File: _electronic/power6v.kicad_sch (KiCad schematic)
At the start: 19 parts

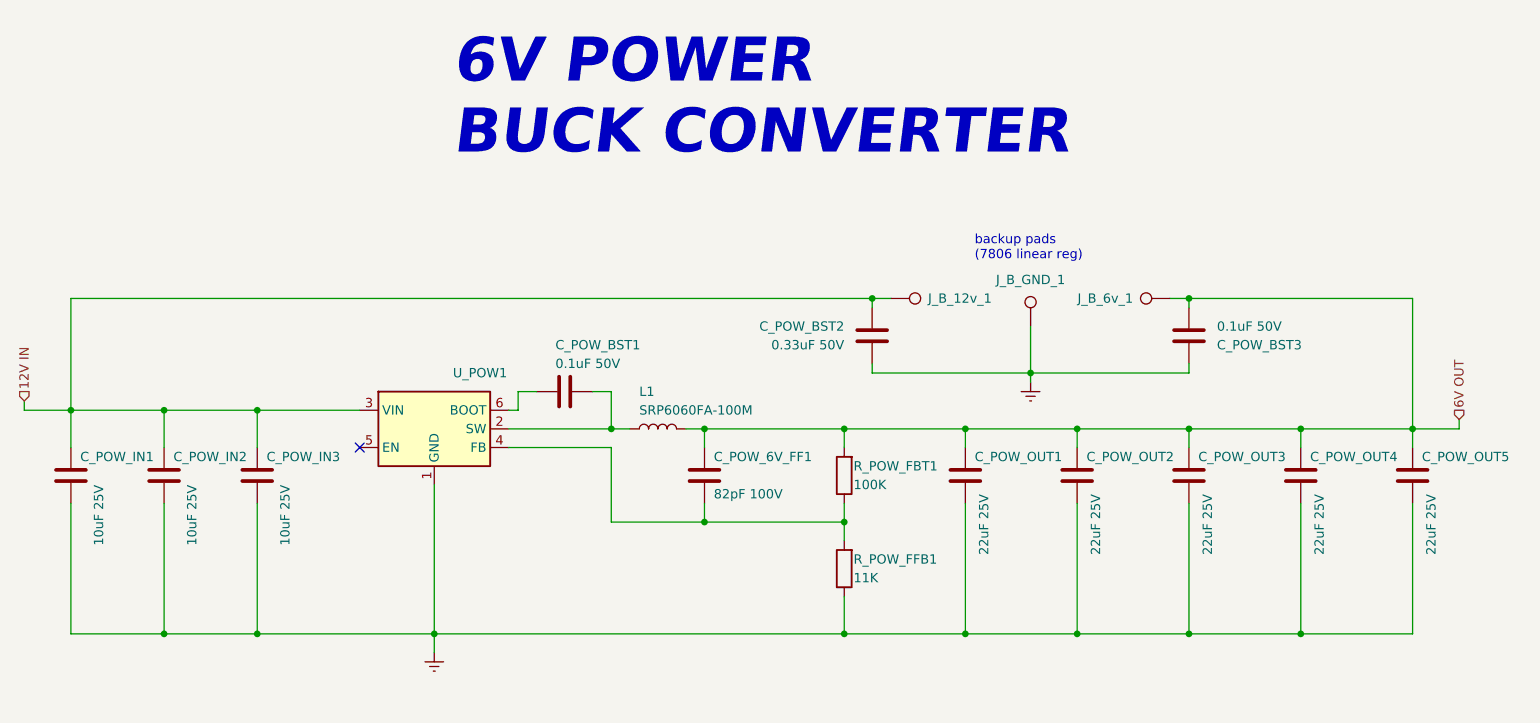
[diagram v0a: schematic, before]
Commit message: led resistor revision, b.o.m. and pcb anotation
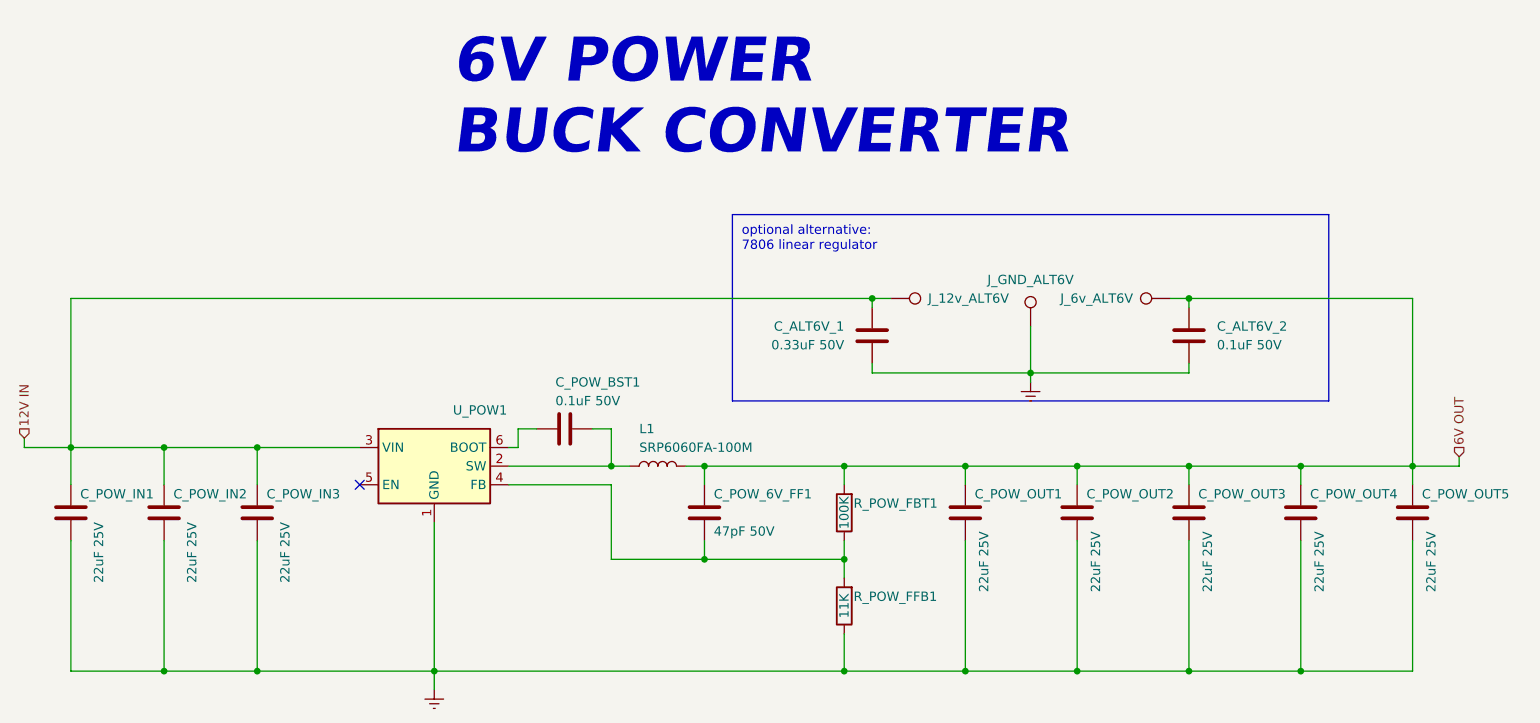
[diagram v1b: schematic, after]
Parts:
- C_ALT6V_1: renamed from C_POW_BST2; now left out of the parts list
- C_ALT6V_2: renamed from C_POW_BST3; now left out of the parts list
- C_POW_6V_FF1: value 82pF 100V -> 47pF 50V; # VJ0603A820JXBAC -> CGA3E2C0G1H470J080AA
- C_POW_IN1, C_POW_IN2, C_POW_IN3: value 10uF 25V -> 22uF 25V; # (none) -> C3225X7R1E226M250AB
- R_POW_FBT1: # CHP0603AFX-1003ELF -> ERJ-3EKF1003V
- R_POW_FFB1: # CRCW060311K0JNEAHP -> ERJ-3EKF1102V
- renumbered J_B_12v_1 to J_12v_ALT6V, J_B_6v_1 to J_6v_ALT6V, J_B_GND_1 to J_GND_ALT6V
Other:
- note added: "optional alternative: 7806 linear regulator"
- note removed: "backup pads (7806 linear reg)"
- moved on the sheet: C_POW_6V_FF1, C_POW_BST1, C_POW_IN1, C_POW_IN2, C_POW_IN3, C_POW_OUT1, C_POW_OUT2, C_POW_OUT3, C_POW_OUT4, C_POW_OUT5, L1, R_POW_FBT1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

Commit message: schematics and pcb cleanup
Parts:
- renumbered J_12v_ALT6V to J_12v_ALT6V1, J_6v_ALT6V to J_6v_ALT6V1, J_GND_ALT6V to J_GND_ALT6V1
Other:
- note added: "alternative 6V output: 7806 linear regulator"
- note removed: "optional alternative: 7806 linear regulator"
- title: E-TKT -> E-TKT v1.0
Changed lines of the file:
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@@
   (paper "A4")
   (title_block
-    (title "E-TKT")
-    (date "2022-07-21")
-    (rev "3")
+    (title "E-TKT v1.0")
+    (date "2022-09-29")
+    (rev "4")
     (company "Andrei Speridiao")
   )
@@
     (stroke (width 0) (type default) (color 0 0 0 0))
   )
-  (text "optional alternative:\n7806 linear regulator" (at 149.86 67.31 0)
+  (text "alternative 6V output:\n7806 linear regulator" (at 149.86 67.31 0)
     (effects (font (size 1.27 1.27)) (justify left bottom))
   )
@@
   (symbol (lib_id "Connector:TestPoint") (at 170.18 73.66 270) (unit 1)
     (in_bom yes) (on_board yes)
-    (property "Reference" "J_12v_ALT6V" (id 0) (at 175.26 73.66 90)
+    (property "Reference" "J_12v_ALT6V1" (id 0) (at 175.26 73.66 90)
       (effects (font (size 1.27 1.27)) (justify left))
     )
@@
   (symbol (lib_id "Connector:TestPoint") (at 189.23 77.47 0) (unit 1)
     (in_bom yes) (on_board yes)
-    (property "Reference" "J_GND_ALT6V" (id 0) (at 189.23 71.12 0))
+    (property "Reference" "J_GND_ALT6V1" (id 0) (at 189.23 71.12 0))
     (property "Value" "TestPoint" (id 1) (at 189.23 72.39 90)
       (effects (font (size 1.27 1.27)) (justify left) hide)
@@
   (symbol (lib_id "Connector:TestPoint") (at 208.28 73.66 90) (unit 1)
     (in_bom yes) (on_board yes)
-    (property "Reference" "J_6v_ALT6V" (id 0) (at 203.2 73.66 90)
-      (effects (font (size 1.27 1.27)) (justify left))
-    )
+    (property "Reference" "J_6v_ALT6V1" (id 0) (at 203.2 73.66 90)
+      (effects (font (size 1.27 1.27)) (justify left))
+    )
